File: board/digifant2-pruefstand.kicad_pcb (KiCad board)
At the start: 2 copper layers, 144 x 114 mm, 48 parts, among them J0 VW ECU HARNESS, J1 12V BENCH IN, J2 IDLE VALVE N71, J3 OLED / UI I2C, Q1 2N7002, Q2 P-MOS -30V >=5A, Q3 2N7002, SW1 PUSH, SW2 PUSH, SW3 PUSH, U1 INA226 (0x40), U2 MCP4728 (0x60), U3 INA226 (0x41), U4 AD9833, U5 Raspberry Pi Pico, Y1 25MHz

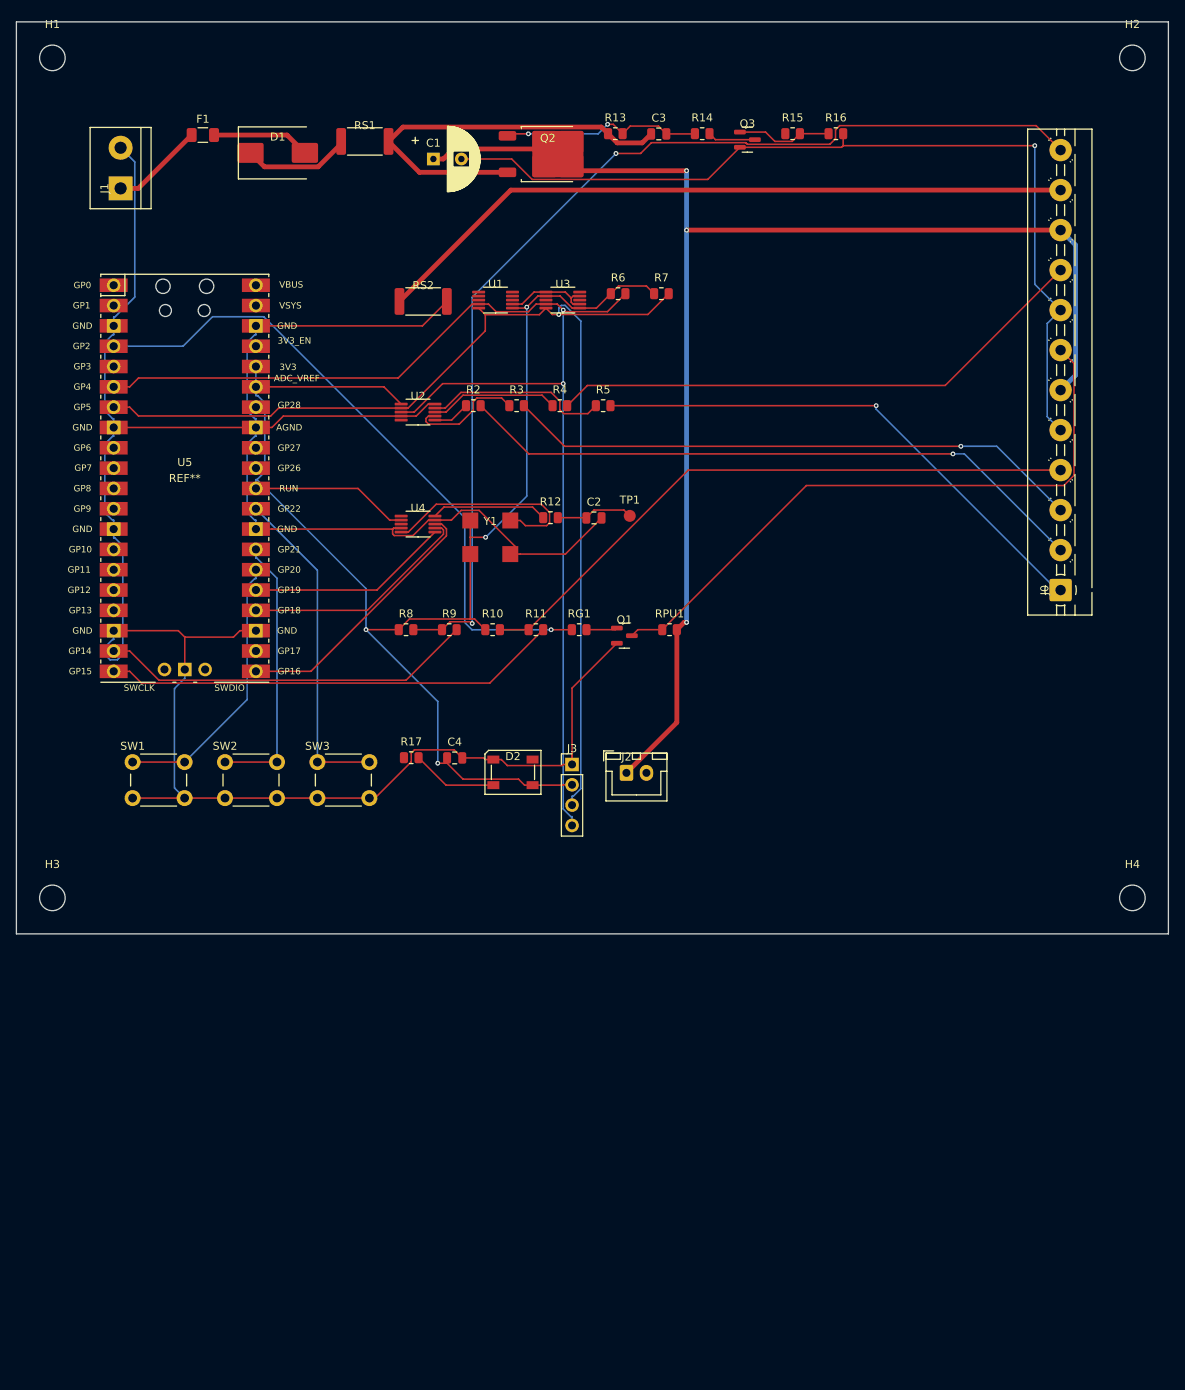
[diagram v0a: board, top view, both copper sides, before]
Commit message: Verify VW pinout; add throttle switches, AFM ref sense, bus-voltage read
- verified the harness against the cabby-info.com Digifant II 25-pin reference;
  DESIGN.md now marks each pin confirmed / flagged (VW-8-vs-18 crank, VW-6/11
  idle-vs-WOT unresolved)
- J0 -> 15-pos terminal block; break out VW-6/11 (throttle switches) and VW-17
- throttle_switches(): Q4/Q5 open-drain emulate the idle + WOT micro-switches
  on GP6/GP7, fail-safe open
- afm_ref_sense(): R20/R21 divider + C5 feed VW-17 into GP26/ADC0 so the LMM
  sim can be scaled ratiometrically
- U1 VBUS moved to the shunt load side -> reads the ECU supply voltage;
  U3 VBUS on the valve supply rail -> reads valve feed voltage
- mounting holes flagged board-only (no more extra_footprint DRC)

Co-Authored-By: Claude Sonnet 5 <noreply@anthropic.com>
Claude-Session: https://claude.ai/code/session_01XcEuUwwCT37oProAm8HYeY
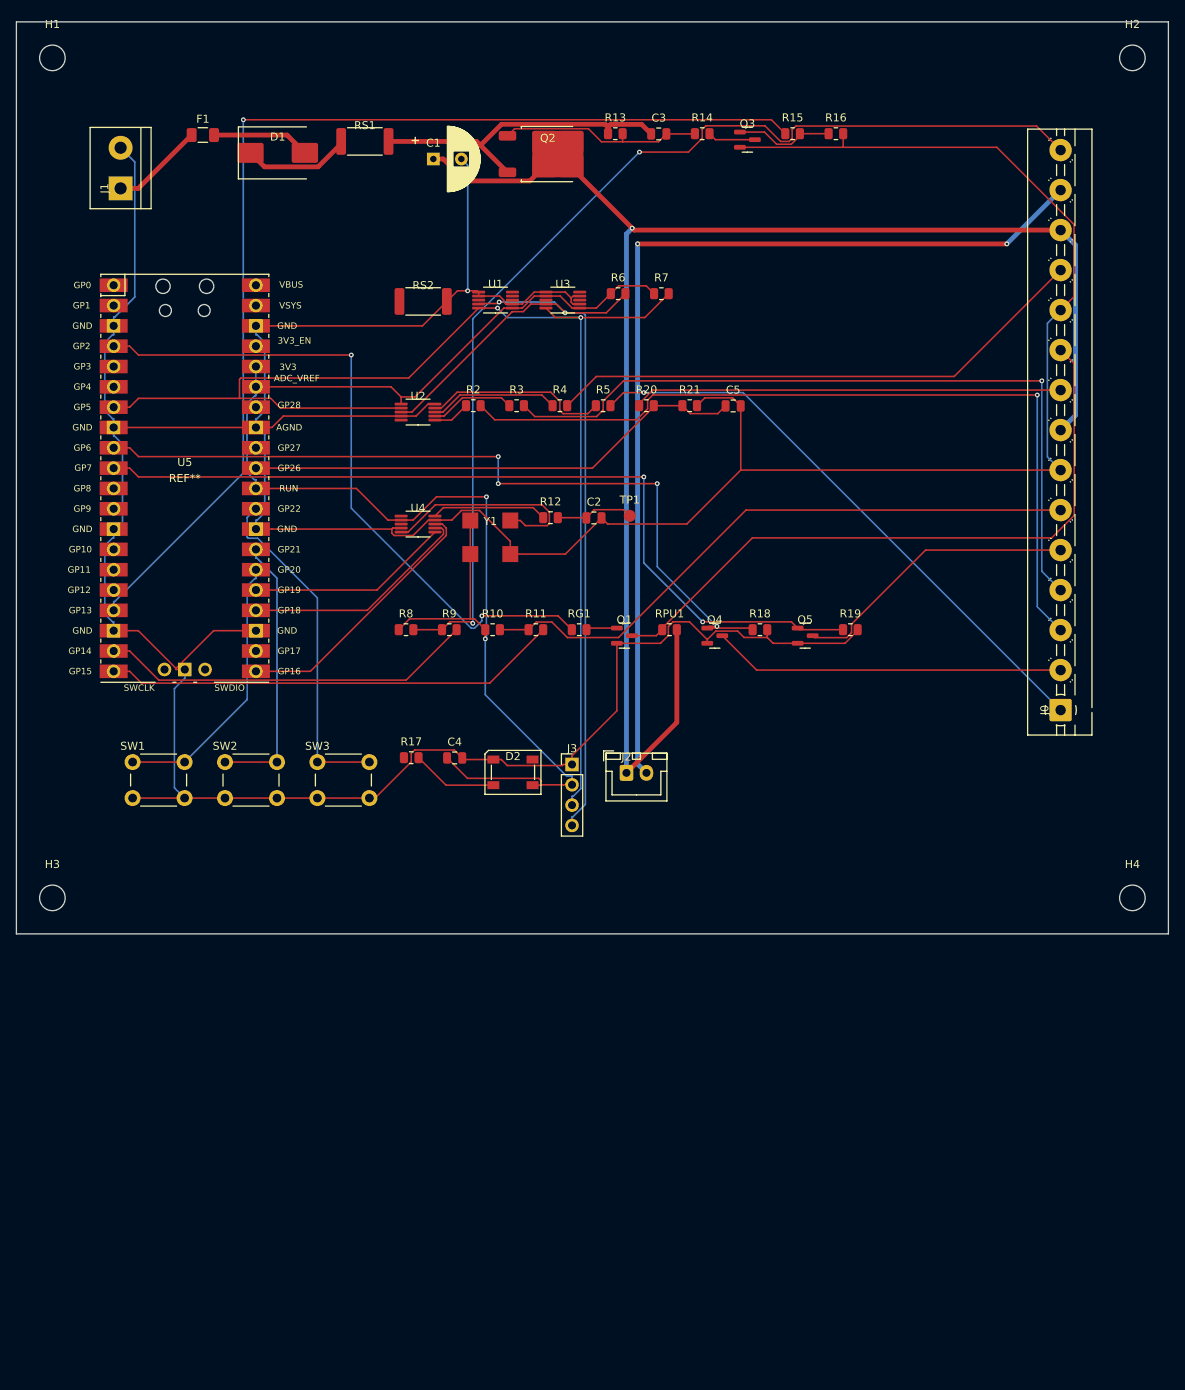
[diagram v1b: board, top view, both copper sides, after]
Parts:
- added C5: 100nF, Capacitor_SMD:C_0805_2012Metric, F.Cu at (89.6, 48.0)
- added Q4: 2N7002, Package_TO_SOT_SMD:SOT-23, F.Cu at (87.3, 76.7)
- added Q5: 2N7002, Package_TO_SOT_SMD:SOT-23, F.Cu at (98.6, 76.7)
- added R18: 100k, Resistor_SMD:R_0805_2012Metric, F.Cu at (92.9, 76.0)
- added R19: 100k, Resistor_SMD:R_0805_2012Metric, F.Cu at (104.2, 76.0)
- added R20: 15k, Resistor_SMD:R_0805_2012Metric, F.Cu at (78.8, 48.0)
- added R21: 10k, Resistor_SMD:R_0805_2012Metric, F.Cu at (84.2, 48.0)
- J0: footprint TerminalBlock:TerminalBlock_MaiXu_MX126-5.0-12P_1x12_P5.00mm -> TerminalBlock:TerminalBlock_MaiXu_MX126-5.0-15P_1x15_P5.00mm
- moved J0 15.0 mm to (130.5, 86.0)
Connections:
- J0 pad 10: +12V_ECU_SW -> VW_PIN18
- J0 pad 11: VW_PIN23_VALVE_RETURN -> GND
- J0 pad 12: VW_PIN25 -> VW_PIN21
- J0 pad 2: VW_PIN9 -> VW_PIN6
- J0 pad 3: VW_PIN10 -> VW_PIN9
- J0 pad 4: VW_PIN12 -> VW_PIN10
- J0 pad 5: GND -> VW_PIN11
- J0 pad 6: +12V_ECU_SW -> VW_PIN12
- J0 pad 7: VW_PIN18 -> GND
- J0 pad 8: GND -> +12V_ECU_SW
- J0 pad 9: VW_PIN21 -> VW_PIN17
- U1 pad 8: +12V_POST_D1 -> +12V_ECU
- U3 pad 8: VW_PIN23_VALVE_RETURN -> +12V_ECU_SW
- U5 pad 10: unconnected-(U5-Pad10-Pad10) -> GP7_THROTTLE_WOT_SW
- U5 pad 31: unconnected-(U5-Pad31-Pad31) -> GP26_AFM_REF_ADC
- U5 pad 9: unconnected-(U5-Pad9-Pad9) -> GP6_THROTTLE_IDLE_SW
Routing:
- net GP13_ECU_PWR_EN: track 0.00 -> 136.6 mm, vias 0 -> 1
- net GP7_THROTTLE_WOT_SW: track 0.00 -> 105.8 mm, vias 0 -> 2
- net GP6_THROTTLE_IDLE_SW: track 0.00 -> 99.8 mm, vias 0 -> 4
- net GND: track 461.4 -> 556.9 mm
- net GP26_AFM_REF_ADC: track 0.00 -> 62.8 mm
- net VW_PIN17: track 0.00 -> 53.6 mm
- net VW_PIN6: track 0.00 -> 44.1 mm
- net I2C_SDA: track 157.1 -> 113.7 mm
- net VW_PIN11: track 0.00 -> 36.2 mm
- net VW_PIN23_VALVE_RETURN: track 88.4 -> 122.2 mm, vias 0 -> 2
- net VW_PIN9: track 80.0 -> 102.8 mm
- net VW_PIN10: track 72.5 -> 94.9 mm
- net I2C_SCL: track 144.7 -> 164.7 mm, vias 1 -> 2
- net +12V_ECU_SW: track 186.8 -> 205.5 mm, vias 3 -> 1
- net +12V_ECU: track 51.3 -> 40.5 mm
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
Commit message: Add GPIO open-circuit switches for the lambda and both temp sensors
U6-U8 (TS5A3159A SPDT, ~1 ohm) in series with the intake-air NTC, coolant
NTC and lambda DAC outputs. GPIO high = sensor connected, low = COM floats to
the open NC pin so the ECU sees an open sensor and should fault. R22-R24 pull
the controls up (connected at power-on). Lambda series R 220R -> 1k so it looks
less like an ideal source. GP8/GP9/GP11.

Also: min_hole_clearance 0.25 -> 0.15 (freerouting put a via near the Pico NPTH).

Co-Authored-By: Claude Sonnet 5 <noreply@anthropic.com>
Claude-Session: https://claude.ai/code/session_01XcEuUwwCT37oProAm8HYeY
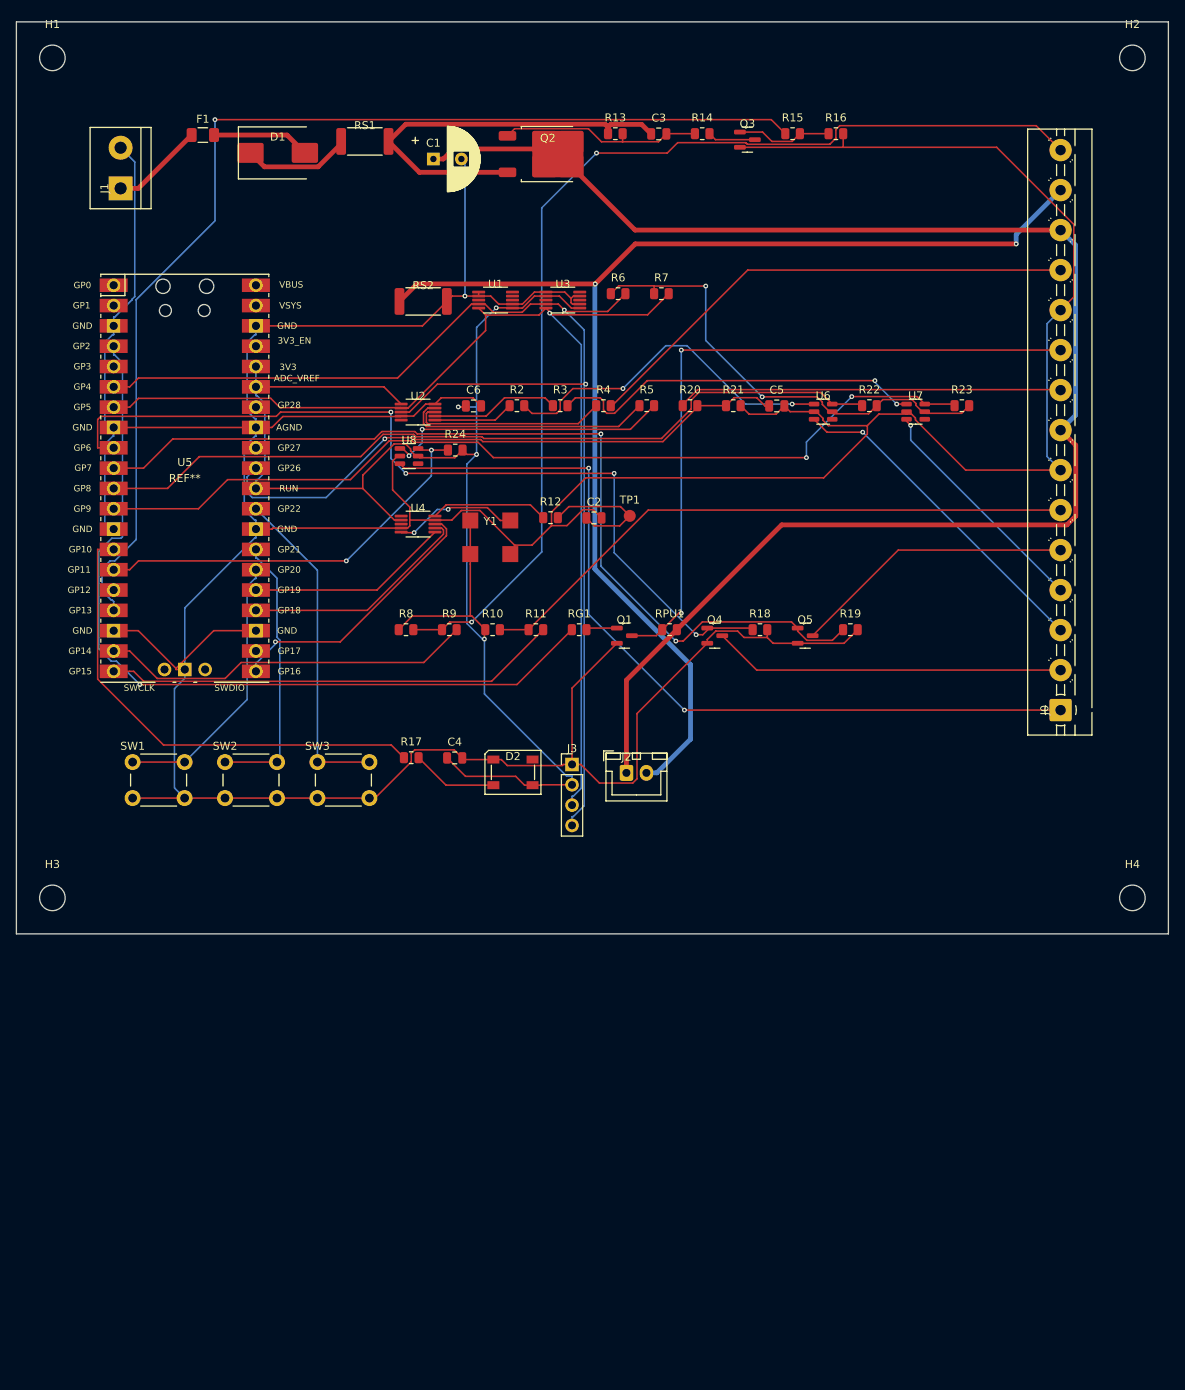
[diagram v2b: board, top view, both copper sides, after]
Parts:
- added C6: 100nF, Capacitor_SMD:C_0805_2012Metric, F.Cu at (57.1, 48.0)
- added R22: 100k, Resistor_SMD:R_0805_2012Metric, F.Cu at (106.6, 48.0)
- added R23: 100k, Resistor_SMD:R_0805_2012Metric, F.Cu at (118.2, 48.0)
- added R24: 100k, Resistor_SMD:R_0805_2012Metric, F.Cu at (54.9, 53.5)
- added U6: TS5A3159A, Package_TO_SOT_SMD:SOT-23-6, F.Cu at (100.8, 48.7)
- added U7: TS5A3159A, Package_TO_SOT_SMD:SOT-23-6, F.Cu at (112.4, 48.7)
- added U8: TS5A3159A, Package_TO_SOT_SMD:SOT-23-6, F.Cu at (49.1, 54.3)
- R5: value 220R -> 1k
- moved C5 5.45 mm to (95.0, 48.0)
- moved R20 5.45 mm to (84.2, 48.0)
- moved R4 5.45 mm to (73.4, 48.0)
- moved R5 5.45 mm to (78.8, 48.0)
- moved R2 5.45 mm to (62.6, 48.0)
- moved R3 5.45 mm to (68.0, 48.0)
- moved R21 5.45 mm to (89.6, 48.0)
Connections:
- R2 pad 2: VW_PIN9 -> R2_SW_IN
- R3 pad 2: VW_PIN10 -> R3_SW_IN
- R5 pad 2: VW_PIN2 -> R5_SW_IN
- U5 pad 11: unconnected-(U5-Pad11-Pad11) -> GP8_AIRTEMP_CONNECT
- U5 pad 12: unconnected-(U5-Pad12-Pad12) -> GP9_WATERTEMP_CONNECT
- U5 pad 15: unconnected-(U5-Pad15-Pad15) -> GP11_LAMBDA_CONNECT
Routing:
- net GP9_WATERTEMP_CONNECT: track 0.00 -> 114.3 mm, vias 0 -> 2
- net GP8_AIRTEMP_CONNECT: track 0.00 -> 100.3 mm
- net +3V3: track 191.4 -> 257.7 mm, vias 2 -> 6
- net VW_PIN10: track 94.9 -> 29.3 mm
- net VW_PIN9: track 102.8 -> 41.7 mm
- net GP10_LED_DATA: track 0.00 -> 60.6 mm
- net GND: track 556.9 -> 613.0 mm
- net GP11_LAMBDA_CONNECT: track 0.00 -> 51.6 mm, vias 0 -> 2
- net I2C_SDA: track 113.7 -> 161.3 mm
- net R3_SW_IN: track 0.00 -> 47.3 mm, vias 0 -> 2
- net R2_SW_IN: track 0.00 -> 43.8 mm, vias 0 -> 2
- net VW_PIN23_VALVE_RETURN: track 122.2 -> 158.2 mm
- net R5_SW_IN: track 0.00 -> 35.8 mm, vias 0 -> 2
- net VW_PIN2: track 73.4 -> 106.1 mm, vias 1 -> 2
- net I2C_SCL: track 164.7 -> 143.1 mm, vias 2 -> 1
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
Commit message: Rotate D1 180deg so its power-chain traces don't route around it
Co-Authored-By: Claude Sonnet 5 <noreply@anthropic.com>
Claude-Session: https://claude.ai/code/session_01XcEuUwwCT37oProAm8HYeY
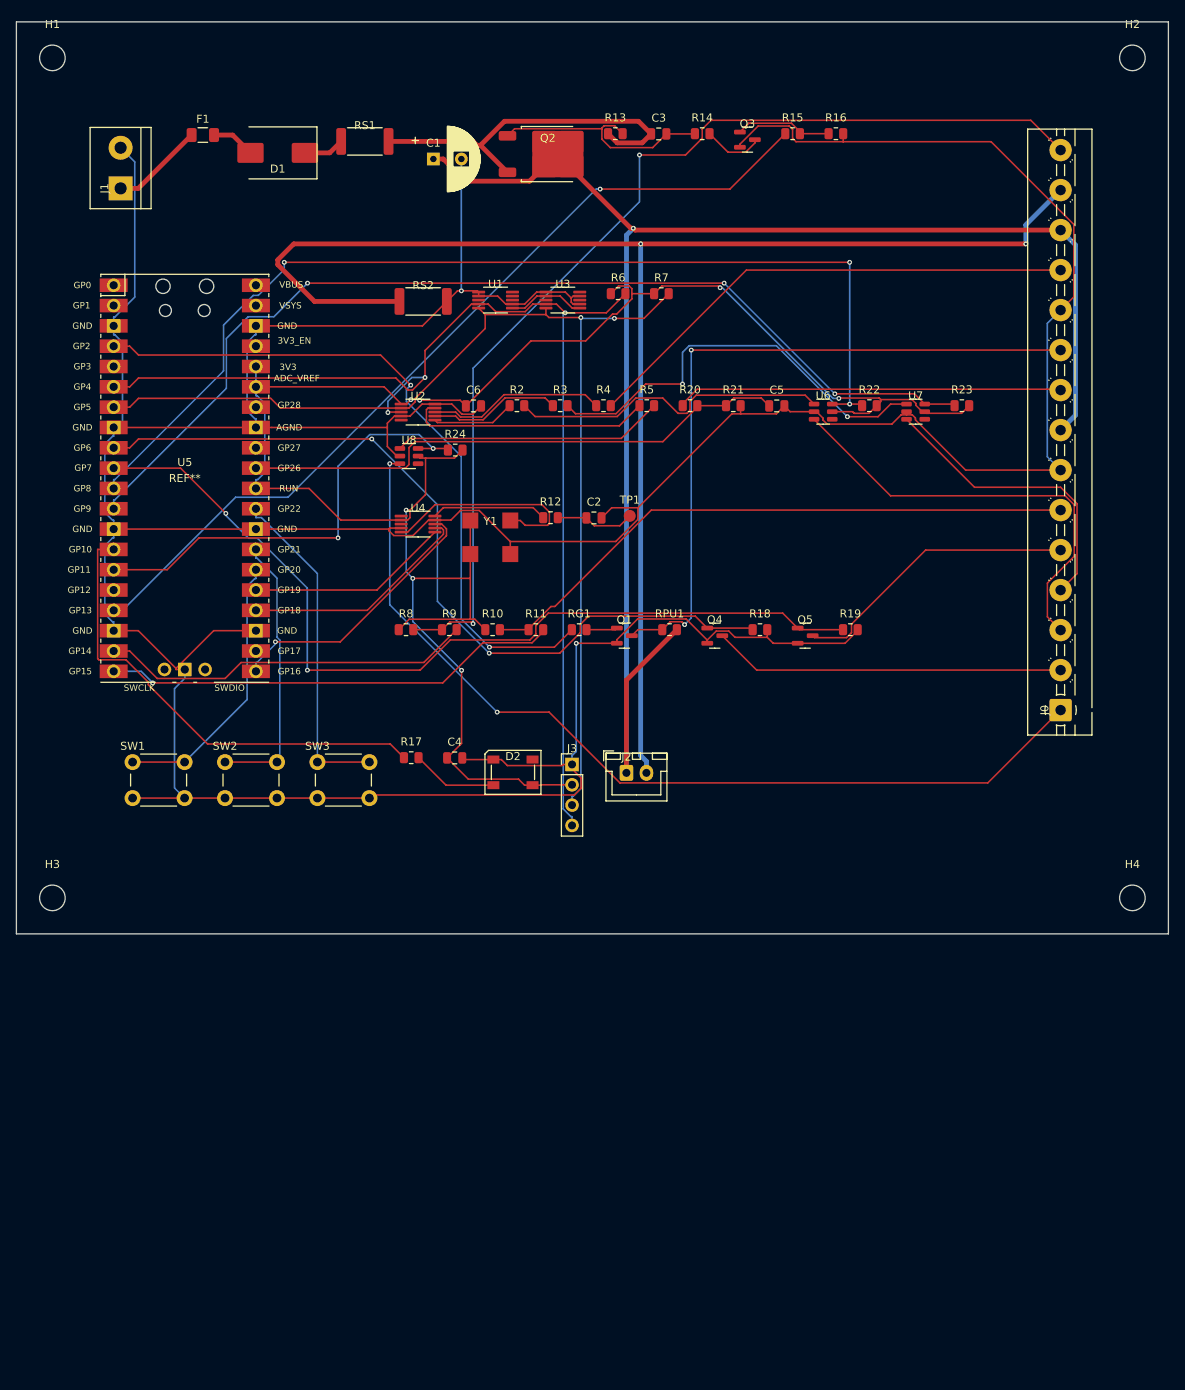
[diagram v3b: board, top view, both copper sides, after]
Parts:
- turned D1 to 180 degrees
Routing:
- net GP13_ECU_PWR_EN: track 140.2 -> 108.6 mm
- net GP8_AIRTEMP_CONNECT: track 100.3 -> 129.8 mm, vias 0 -> 3
- net VW_PIN23_VALVE_RETURN: track 158.2 -> 187.0 mm
- net GND: track 613.0 -> 592.3 mm, vias 1 -> 2
- net GP2_CRANK: track 104.1 -> 87.6 mm, vias 1 -> 2
- net I2C_SDA: track 161.3 -> 147.4 mm, vias 2 -> 3
- net GP9_WATERTEMP_CONNECT: track 114.3 -> 127.4 mm, vias 2 -> 3
- net VW_PIN9: track 41.7 -> 54.7 mm, vias 1 -> 0
- net N$3: track 15.6 -> 27.0 mm, vias 2 -> 0
- net VW_PIN2: track 106.1 -> 115.8 mm
- net +12V_POST_D1: track 13.5 -> 5.12 mm
- net VW_PIN10: track 29.3 -> 37.3 mm, vias 1 -> 0
- net GP6_THROTTLE_IDLE_SW: track 109.2 -> 101.7 mm, vias 4 -> 2
- net +12V_PROT: track 12.3 -> 5.48 mm
- net U4_LOAD: track 16.4 -> 9.92 mm
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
